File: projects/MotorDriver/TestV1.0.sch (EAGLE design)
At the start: 56 parts, among them IC1 7805TV, IC2 7812TV, J1 ARDUINO_UNO_R3, Q1 IRF9530, Q2 IRF9530, Q3 IRF9530, Q4 IRF9530, Q5 IRF9530, Q6 IRF9530

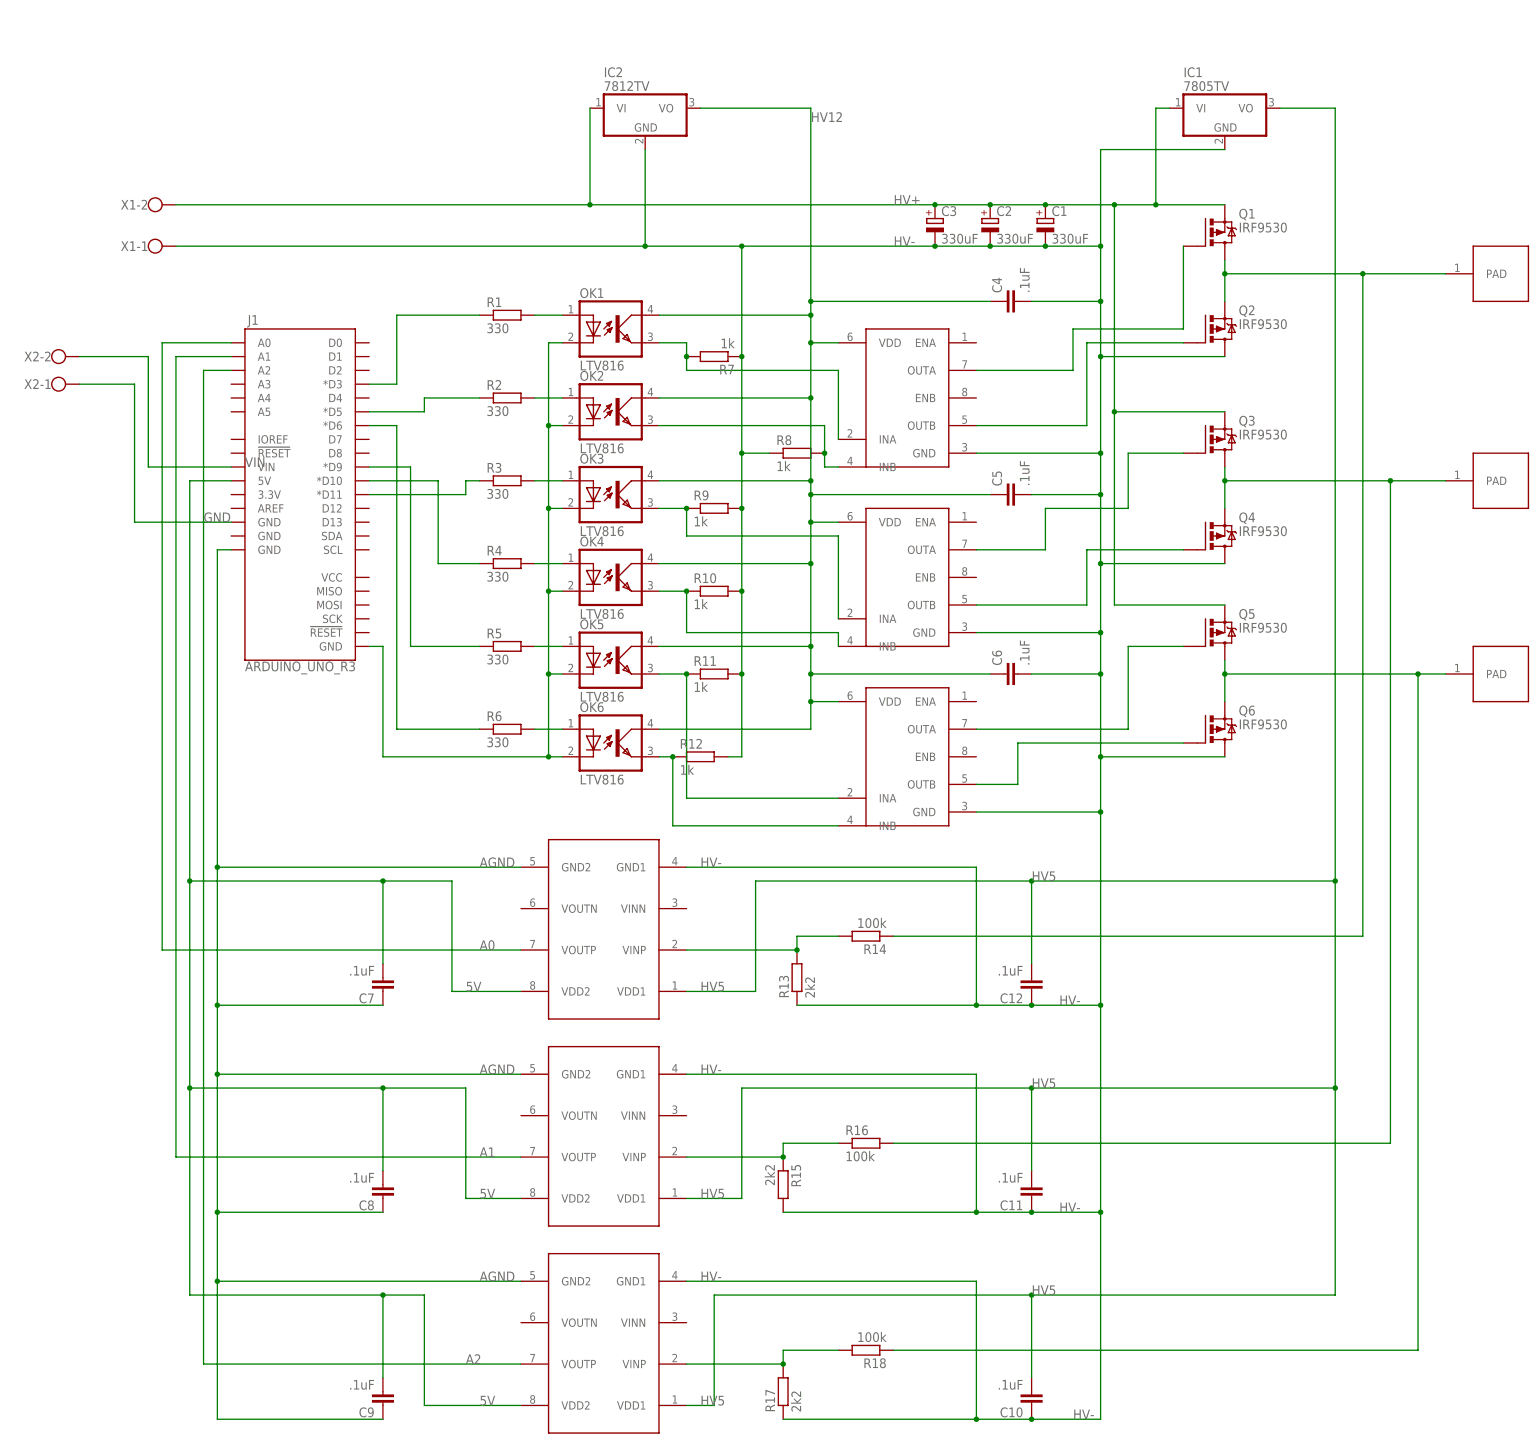
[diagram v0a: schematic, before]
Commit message: added hall effect test board
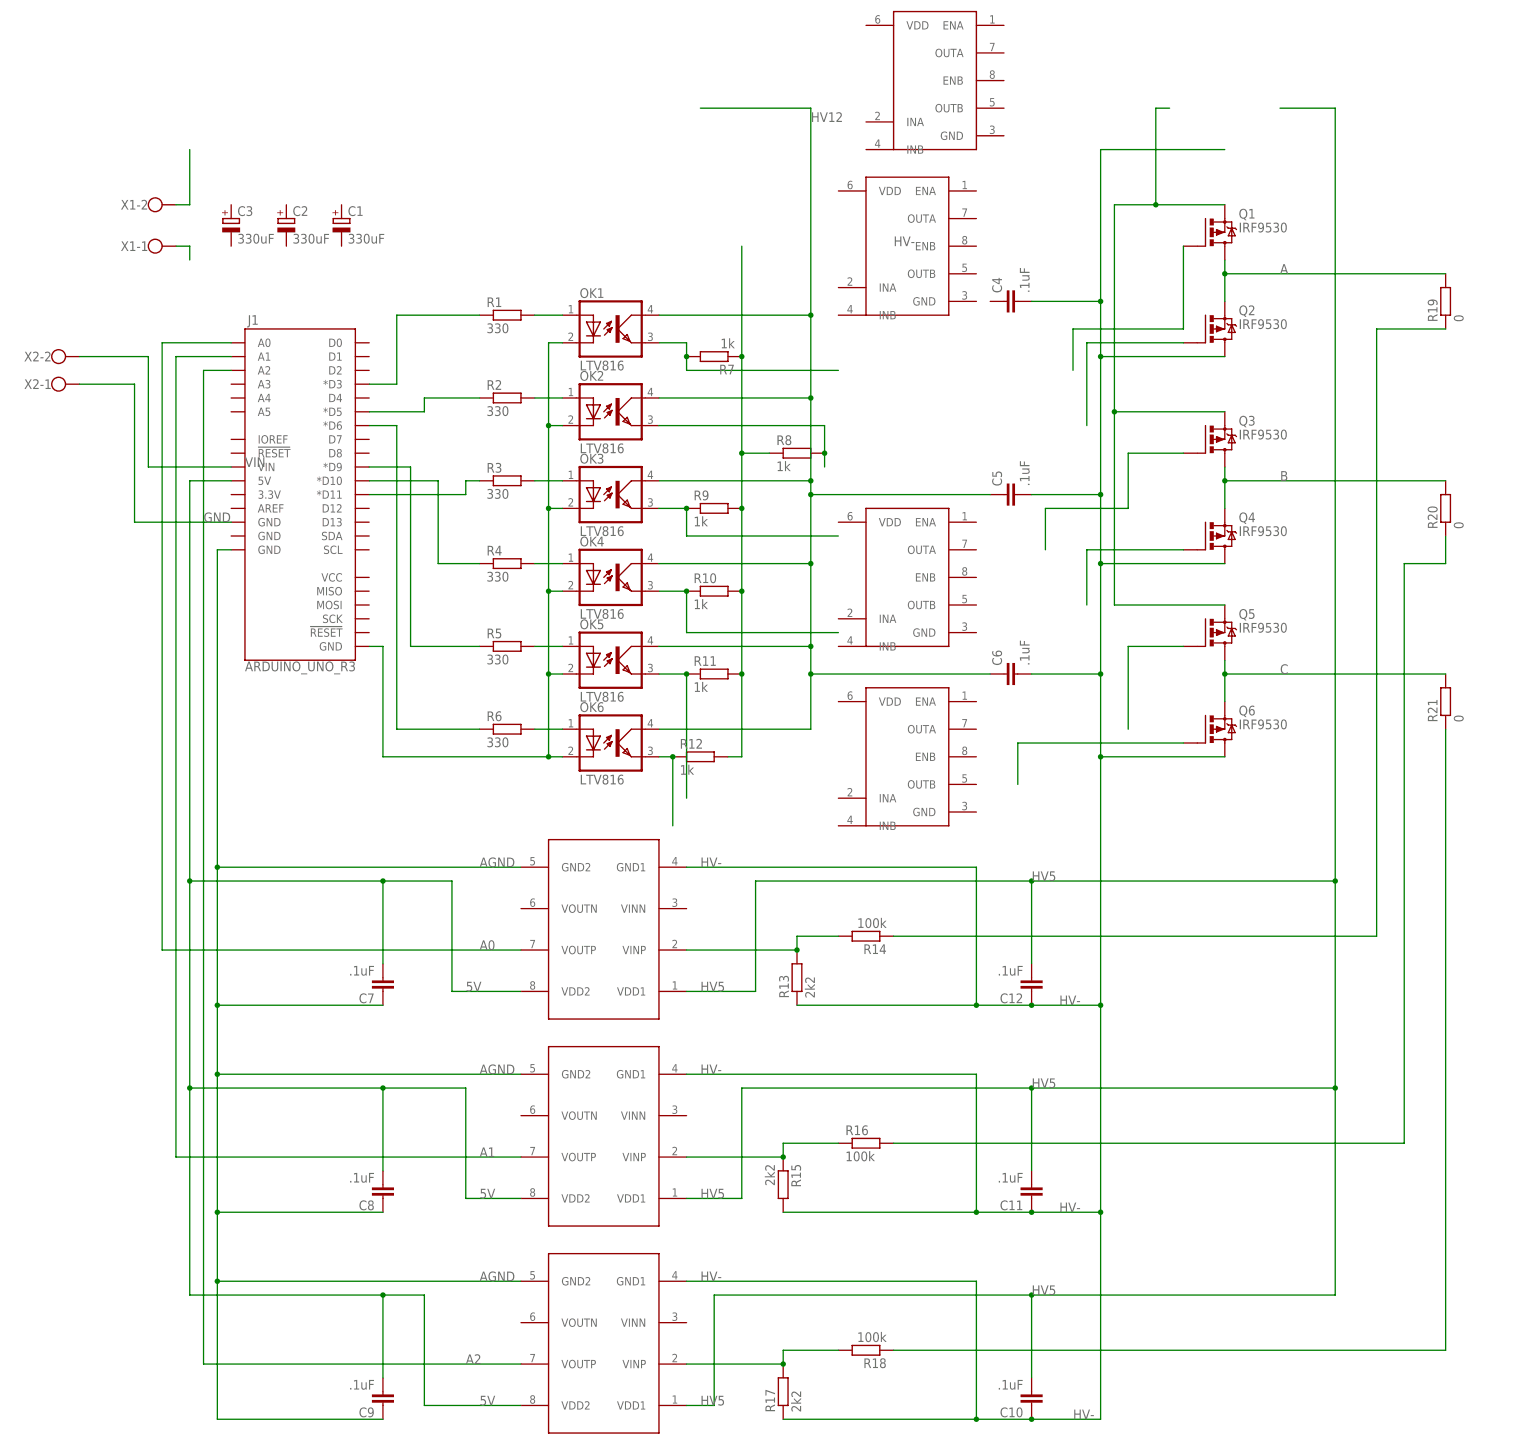
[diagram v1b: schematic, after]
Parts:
- removed IC1: 7805TV, linear:7805TV
- removed IC2: 7812TV, linear:7812TV
- removed U$1: MAX17604, st-microelectronics:MAX17604
- removed U$4, U$5, U$6: WIRE_SOLDER_PAD, ISCTRainingProgram:WIRE_SOLDER_PAD
- added MAX17604_A, MAX17604_B: MAX17604, st-microelectronics:MAX17604
- added R19, R20, R21: 0, eagle-ltspice:RR0603
- renumbered U$2 to MAX17604_C, U$3 to MAX17604_D
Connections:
- removed net N$3: Q1.D, Q2.S, R14.1, U$4.PAD
- removed net N$4: Q3.D, Q4.S, R16.2, U$5.PAD
- removed net N$5: Q5.D, Q6.S, R18.1, U$6.PAD
- new net A: Q1.D, Q2.S, R19.2
- new net A_MINOR: R14.1, R19.1
- new net B: Q3.D, Q4.S, R20.2
- new net B_MINOR: R16.2, R20.1
- new net C: Q5.D, Q6.S, R21.2
- new net C_MINOR: R18.1, R21.1
- new net N$30: X1-2.KL
- new net N$36: R10.2, R11.2, R12.2, R7.1, R8.1, R9.2
- new net N$38: X1-1.KL
- net HV+: no longer C1.+, C2.+, C3.+, IC1.VI, IC2.VI, X1-2.KL
- net HV-: no longer C1.-, C2.-, C3.-, IC1.GND, IC2.GND, MAX17604_C.GND, MAX17604_D.GND, R10.2, R11.2, R12.2, R7.1, R8.1, R9.2, U$1.GND, X1-1.KL
- net HV12: no longer C4.1, IC2.VO, MAX17604_C.VDD, MAX17604_D.VDD, U$1.VDD
- net HV5: no longer IC1.VO
- net N$1: no longer U$1.OUTA
- net N$10: no longer U$1.INA
- net N$11: no longer U$1.INB
- net N$12: no longer MAX17604_C.INA
- net N$13: no longer MAX17604_C.INB
- net N$14: no longer MAX17604_D.INA
- net N$15: no longer MAX17604_D.INB
- net N$2: no longer U$1.OUTB
- net N$6: no longer MAX17604_C.OUTA
- net N$7: no longer MAX17604_C.OUTB
- net N$8: no longer MAX17604_D.OUTA
- net N$9: no longer MAX17604_D.OUTB
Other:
- moved on the sheet: C1, C2, C3
